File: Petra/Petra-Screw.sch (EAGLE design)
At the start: 25 parts, among them J2 AVR_SPI_PRG_6NS, U1 MIC5219 5V, Y1 16MHz

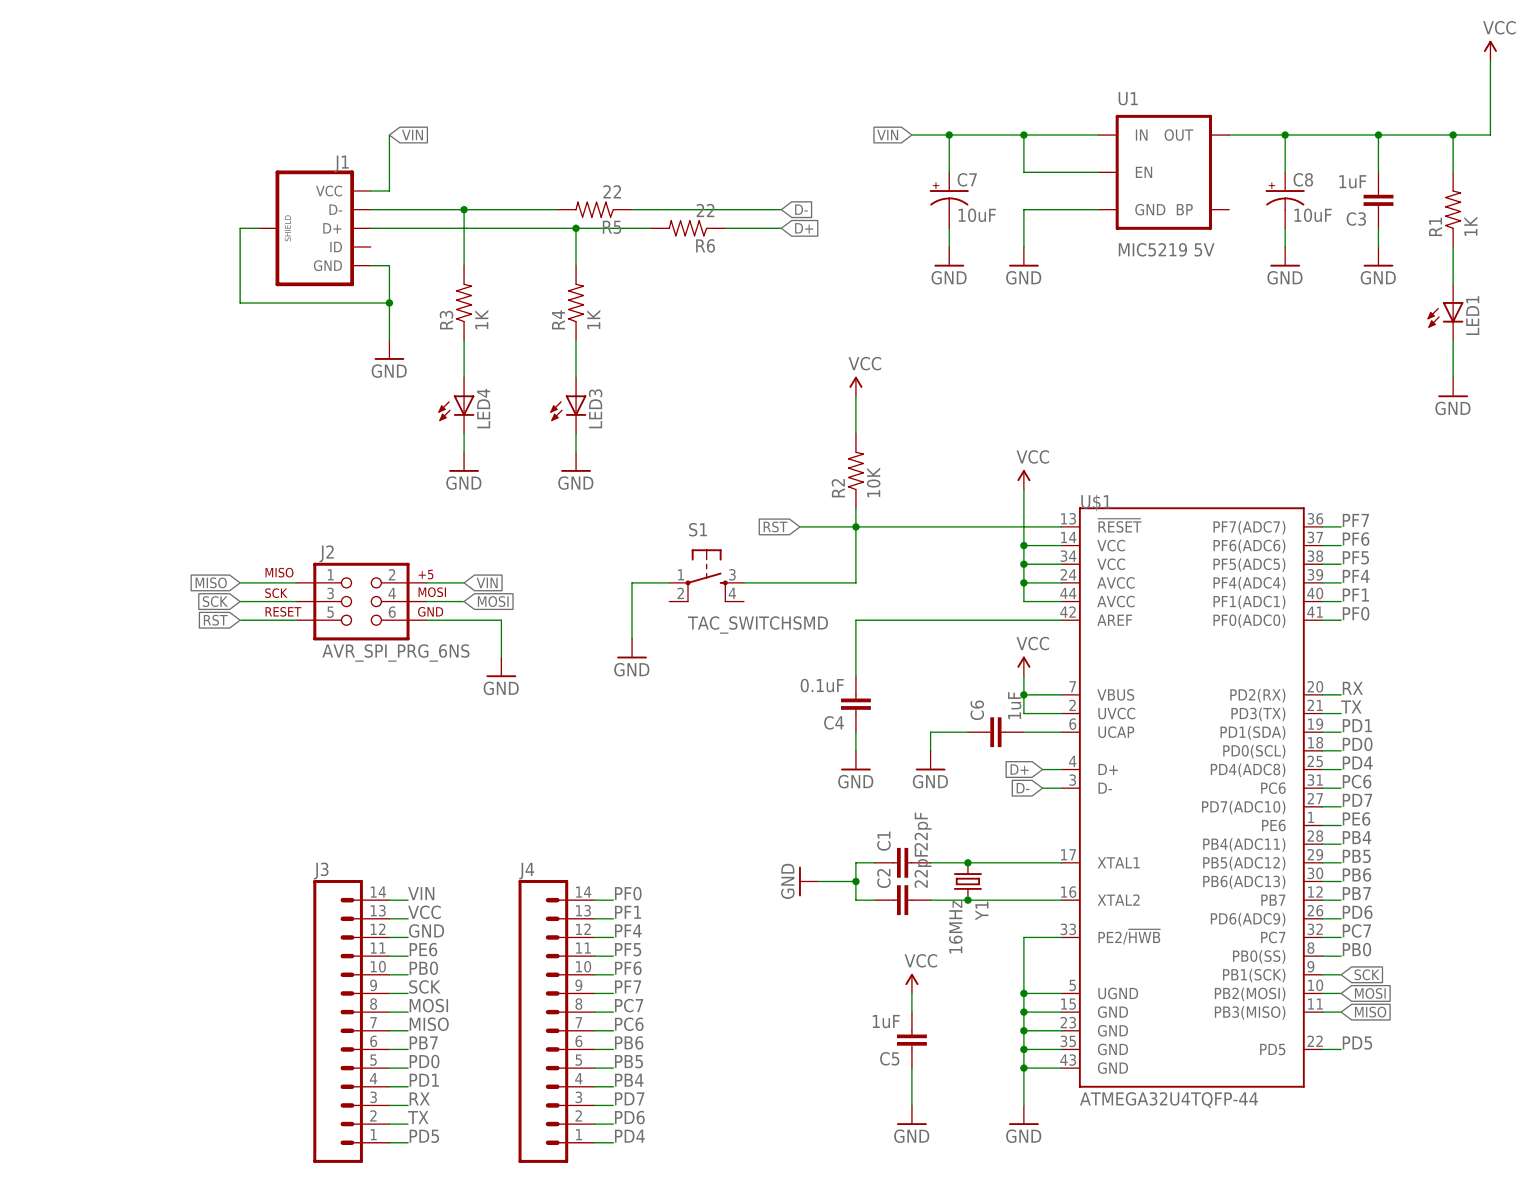
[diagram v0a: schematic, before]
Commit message: Created Screw Terminal Board. Cleaned up folder structure.
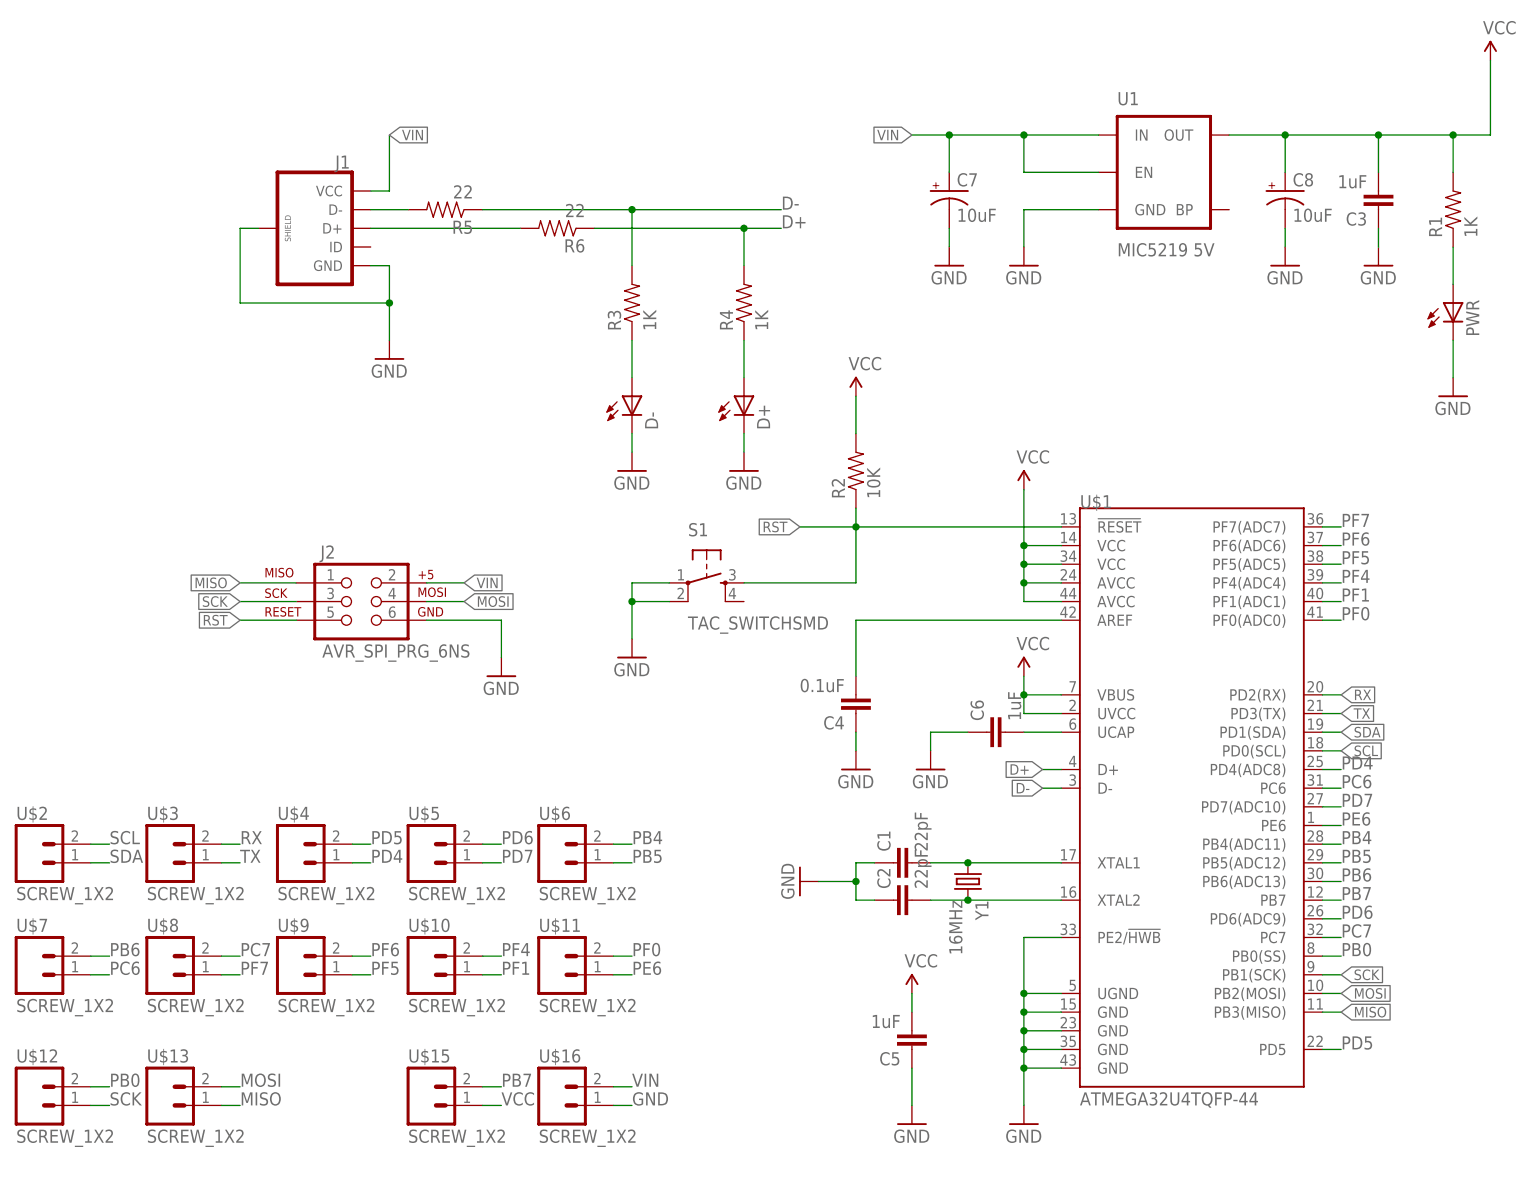
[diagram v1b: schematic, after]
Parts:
- removed J3, J4: (no value), SparkFun-Connectors:M14
- removed LED3, LED4: (no value), led:LEDCHIP-LED0805
- added D+, D-: (no value), led:LEDCHIP-LED0805
- added U$10, U$11, U$12, U$13, U$15, U$16, U$2, U$3, U$4, U$5, U$6, U$7, U$8, U$9: SCREW_1X2, PartsYouNeed:SCREW_1X2
- renumbered LED1 to PWR
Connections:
- removed net A: J1.D-, R3.2, R5.2
- removed net B: J1.D+, R4.2, R6.2
- removed net PD0: J3.5, U$1.PD0(SCL)
- removed net PD1: J3.4, U$1.PD1(SDA)
- new net N$5: J1.D-, R5.2
- new net N$6: J1.D+, R6.2
- new net SCL: U$1.PD0(SCL), U$2.2
- new net SDA: U$1.PD1(SDA), U$2.1
- net D+: now also R4.2
- net D-: now also R3.2
- net GND: now also D+.C, D-.C, S1.2, U$16.1; no longer J3.12, LED3.C, LED4.C
- net MISO: now also U$13.1; no longer J3.7
- net MOSI: now also U$13.2; no longer J3.8
- net N$11: now also D-.A; no longer LED4.A
- net N$9: now also D+.A; no longer LED3.A
- net PB0: now also U$12.2; no longer J3.10
- net PB4: now also U$6.2; no longer J4.4
- net PB5: now also U$6.1; no longer J4.5
- net PB6: now also U$7.2; no longer J4.6
- net PB7: now also U$15.2; no longer J3.6
- net PC6: now also U$7.1; no longer J4.7
- net PC7: now also U$8.2; no longer J4.8
- net PD4: now also U$4.1; no longer J4.1
- net PD5: now also U$4.2; no longer J3.1
- net PD6: now also U$5.2; no longer J4.2
- net PD7: now also U$5.1; no longer J4.3
- net PE6: now also U$11.1; no longer J3.11
- net PF0: now also U$11.2; no longer J4.14
- net PF1: now also U$10.1; no longer J4.13
- net PF4: now also U$10.2; no longer J4.12
- net PF5: now also U$9.1; no longer J4.11
- net PF6: now also U$9.2; no longer J4.10
- net PF7: now also U$8.1; no longer J4.9
- net RX: now also U$3.2; no longer J3.3
- net SCK: now also U$12.1; no longer J3.9
- net TX: now also U$3.1; no longer J3.2
- net VCC: now also U$15.1; no longer J3.13
- net VIN: now also U$16.2; no longer J3.14
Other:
- moved on the sheet: R3, R4, R5, R6
